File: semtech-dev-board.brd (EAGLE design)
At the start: 73.4 x 82.5 mm, 62 parts, among them Q1 BSS123, Q2 32MHz, U1 SEMTECH_SX1236, U2 QUALCOMM-TDK_B3588, U3 MIC5219 3.3V, U4 QUALCOMM-TDK_B3710

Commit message: Tuesday D/R
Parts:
- removed C24, C26, C28: 100nF, rcl:C0805
- removed TP7: TEST-POINT, low-gain-radio:2MM-TEST-POINT
- added TP3: TEST-POINT, low-gain-radio:2MM-TEST-POINT
- C11: value 22pF -> 100nF
- C12: value 4.7pF -> 100nF
- C13: value 8.2pF -> 100nF
- C14: value 2.7pF -> 8.2pF
- C15: value ?? -> 10nF
- C16: value 15pF -> 6.8pF
- C17: value ?? -> 5.6pF
- C18: value 6.8pF -> 100nF
- C19: value ?? -> 100nF
- C20: value 8.2pF -> 4.7pF
- C21: value 470pF -> 15pF
- C22: value 5.6pF -> 15pF
- C4: value 100nF -> 470pF
- C5: value 100nF -> 2.7pF
- C6: value 6pF -> 22pF
- C7: value 6pF -> 15pF
- C8: value 10nF -> 8.2pF
- JP1: device pinhead:1X07 -> pinhead:1X02
- JP2: device pinhead:1X04 -> pinhead:1X02
- JP3, JP5: device pinhead:1X02 -> pinhead:1X04
- JP4: device pinhead:1X04 -> pinhead:1X08
- L1: value 33nH -> 12nH; device rcl:L3230M -> rcl:L3225M
- L2: value 33nH -> 10nH; device rcl:L3230M -> rcl:L3225M
- L3: value 10nH -> 33nH; device rcl:L3230M -> rcl:L3225M
- L4: value 3.9nH -> 10nH; device rcl:L3230M -> rcl:L3225P
- L5: value 12nH -> 33nH; device rcl:L1812 -> rcl:L3225P
- L6: device rcl:L3230M -> rcl:L3225M
- L7: value 10nH -> 6.8nH; device rcl:L3230M -> rcl:L3225M
- L8: value 6.8nH -> 3.9nH; device rcl:L3230M -> rcl:L3225M
- R1: value 1k -> 0
- R5: value 0 -> 1k
- U1: value SEMTECH_SX1236 -> MIC5219 3.3V; device low-gain-radio:QFN28 -> SparkFun-IC-Power:SOT23-5
- U2: value QUALCOMM-TDK_B3588 -> QUALCOMM-TDK_B3710
- U3: value MIC5219 3.3V -> QUALCOMM-TDK_B3588; device SparkFun-IC-Power:SOT23-5 -> low-gain-radio:DCC6C
- U4: value QUALCOMM-TDK_B3710 -> SEMTECH_SX1236; device low-gain-radio:DCC6C -> low-gain-radio:QFN28
- moved U3 77.1 mm to (65.5, 75.9), turned to 180 degrees
- moved R2 56.7 mm to (18.3, 11.9), turned to 180 degrees
- moved U4 56.6 mm to (33.0, 23.6), turned to 0 degrees
- moved U2 54.1 mm to (11.4, 75.9)
- moved C22 53.7 mm to (26.2, 24.1), turned to 180 degrees
- moved R3 52.9 mm to (67.1, 40.9)
- moved JP2 51.1 mm to (70.9, 49.3), turned to 90 degrees
- moved C19 50.1 mm to (24.0, 26.5), turned to 180 degrees
- moved C7 42.7 mm to (26.6, 66.9)
- moved C18 39.3 mm to (28.4, 31.8), turned to 90 degrees
- moved C6 38.8 mm to (27.6, 59.5), turned to 90 degrees
- moved C13 38.7 mm to (39.6, 21.3), turned to 270 degrees
- moved JP4 38.4 mm to (37.6, 2.03)
- moved C5 37.3 mm to (27.6, 63.6), turned to 90 degrees
- moved JP3 35.4 mm to (36.6, 40.4), turned to 0 degrees
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- renumbered C23 to C3, C27 to C1, CF1 to P5, Q2 to Y1, S2 to S1, U$1 to P1, U$2 to P2, U$3 to P3, U$4 to P4
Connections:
- removed net DIO0: JP1.2, U1.8
- removed net DIO1: JP1.3, U1.9
- removed net DIO2: JP1.4, U1.10
- removed net DIO3: JP1.5, U1.11
- removed net DIO4: JP1.6, U1.12
- removed net DIO5: JP1.7, U1.13
- new net N$2: JP4.8, U4.13
- new net N$4: JP4.7, U4.12
- new net N$6: JP4.6, U4.11
- new net N$7: JP4.5, U4.10
- new net N$8: JP4.4, U4.9
- new net N$9: JP4.3, U4.8
- net +3V3: now also R4.2, R5.2, TP6.1, U1.5; no longer R1.2, R3.2, TP5.1, U3.5
- net BP: now also C4.1, U1.4; no longer C21.1, U3.4
- net GND: now also C11.2, C13.2, C15.2, C17.2, C19.2, JP1.2, JP2.2, U1.2, U3.P$1, U3.P$3, U3.P$4, U3.P$6, U4.0, U4.15, U4.23, U4.26; no longer C24.2, C26.2, C28.2, C5.2, C6.2, JP3.2, JP5.2, U1.0, U1.15, U1.23, U1.26, U3.2, U4.P$1, U4.P$3, U4.P$4, U4.P$6
- net HFO_PA_HEAD: now also C15.1, JP3.4, L5.2; no longer C9.1, JP4.4, L2.2
- net LED+: now also R3.1; no longer R2.1
- net LFO_PA_HEAD: now also C9.1, JP3.1, L3.2; no longer C8.1, JP4.1, L1.2
- net N$1: now also R2.1, TP4.1, U1.3; no longer R5.1, TP1.1, U3.3
- net N$5: now also U2.P$5; no longer U4.P$5
- net PA_BOOST: now also TP2.1, U4.27; no longer TP7.1, U1.27
- net RFI_HF: now also U3.P$2, U4.21; no longer U1.21, U2.P$2
- net RFI_HF_ANT: now also U3.P$5; no longer U2.P$5
- net RFI_LF: now also U2.P$2, U4.1; no longer U1.1, U4.P$2
- net RFO_HF: now also L8.2, U4.22; no longer L4.2, U1.22
- net RFO_HF_1: now also C14.2; no longer C13.2, C15.1
- net RFO_HF_2: now also C16.1, L7.2; no longer C15.2, C18.1, C19.1, L8.2
- net RFO_HF_OUT: now also C17.1, L7.1; no longer C19.2, C22.1, L8.1
- net RFO_HF_PA: now also C14.1, C20.1, L5.1, L8.1; no longer C12.1, C13.1, L2.1, L4.1
- net RFO_LF: now also L4.1, U4.28; no longer L3.1, U1.28
- net RFO_LF_1: now also C5.1, C6.2, L1.2; no longer C11.2, C14.1, L5.2
- net RFO_LF_2: now also C5.2, C7.1, L1.1, L2.2; no longer C14.2, C16.1, C17.1, L5.1, L7.2
- net RFO_LF_OUT: now also C8.1, L2.1; no longer C17.2, C20.1, L7.1
- net RFO_LF_PA: now also C6.1, L3.1, L4.2; no longer C11.1, L1.1, L3.2
- net RXTX: now also JP2.1, JP4.2, U4.20; no longer JP1.1, JP3.1, U1.20
- net SPI_MISO: now also JP5.2, U4.17; no longer JP2.2, U1.17
- net SPI_MOSI: now also JP5.3, U4.18; no longer JP2.3, U1.18
- net SPI_NSS: now also JP5.4, U4.19; no longer JP2.4, U1.19
- net SPI_SCK: now also JP5.1, U4.16; no longer JP2.1, U1.16
- net SX1236_RST: now also JP4.1, R5.1, TP1.1, U4.7; no longer R1.1, TP4.1, U1.7
- net VBAT: now also C11.1, C12.1, C13.1, R3.2, R4.1, U4.14, U4.24, U4.3; no longer C2.1, C24.1, C26.1, R2.2, R3.1, U1.14, U1.24, U1.3
- net VREG_IN: now also C2.1, R1.2, R2.2, TP5.1, U1.1; no longer C28.1, R4.2, R5.2, TP6.1, U3.1
- net VR_ANA: now also C18.1, U4.2; no longer C4.1, U1.2
- net VR_DIG: now also C19.1, U4.4; no longer C5.1, U1.4
- net VR_PA: now also JP3.2, JP3.3, U4.25; no longer JP4.2, JP4.3, U1.25
- net V_IN: now also JP1.1, R1.1, TP3.1; no longer JP5.1, R4.1, TP2.1
- net XTALA: now also C22.1, U4.5; no longer C7.1, U1.5
- net XTALB: now also C21.1, U4.6; no longer C6.1, U1.6
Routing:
- net DIO5: track 24.7 -> 0.00 mm
- net DIO4: track 23.9 -> 0.00 mm
- net DIO0: track 23.2 -> 0.00 mm
- net DIO3: track 23.1 -> 0.00 mm
- net DIO1: track 22.4 -> 0.00 mm
- net DIO2: track 22.3 -> 0.00 mm
- net RFO_HF_2: track 10.5 -> 6.00 mm
- net VREG_IN: track 11.8 -> 15.6 mm
- net RFO_LF_OUT: track 10.4 -> 7.95 mm
- net RFO_HF_OUT: track 10.3 -> 7.93 mm
- net RXTX: track 141.6 -> 140.6 mm
- net RFO_LF_1: track 5.46 -> 5.97 mm
- added copper zone on layer 2, net GND
- added copper zone on layer 15, net VBAT
- removed copper zone on layer 2, net VBAT
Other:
- board size 73.4 x 82.5 mm -> 73.2 x 82.2 mm

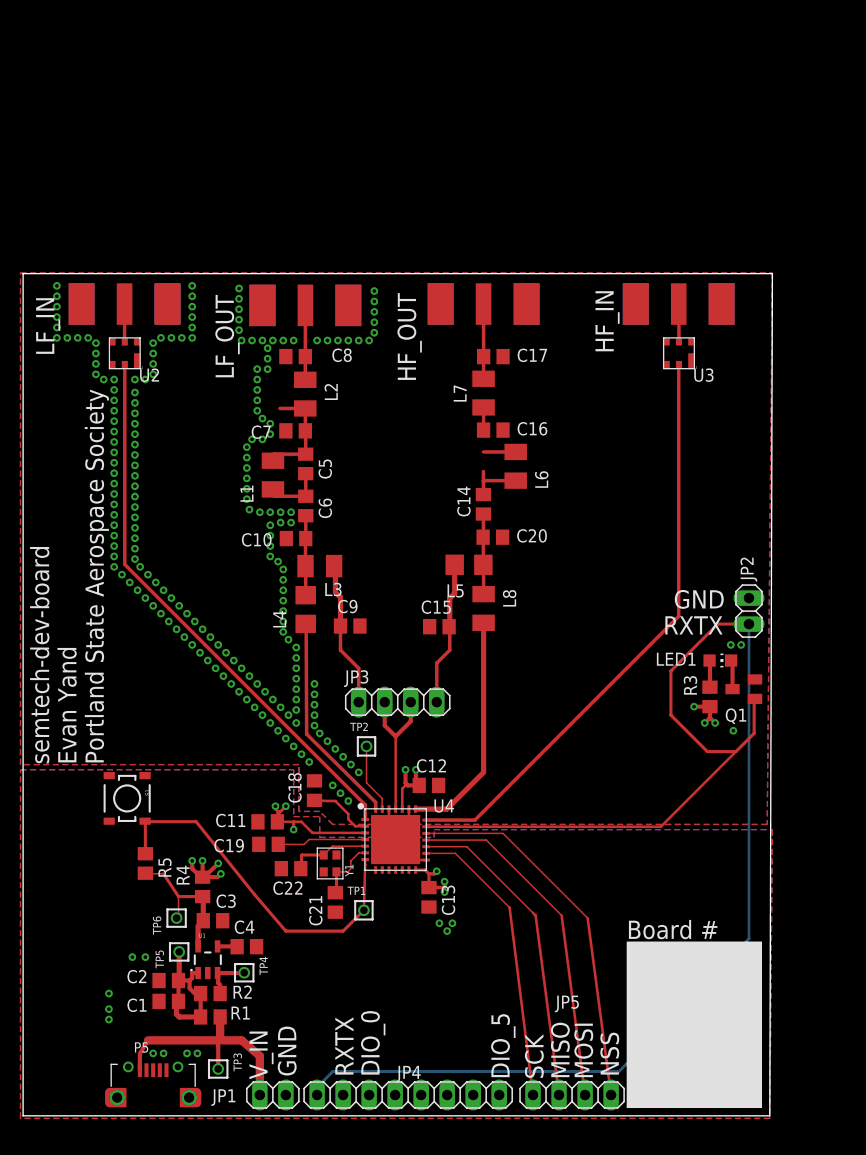
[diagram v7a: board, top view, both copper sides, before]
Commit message: reworked board based on feedback, needs mounting holes
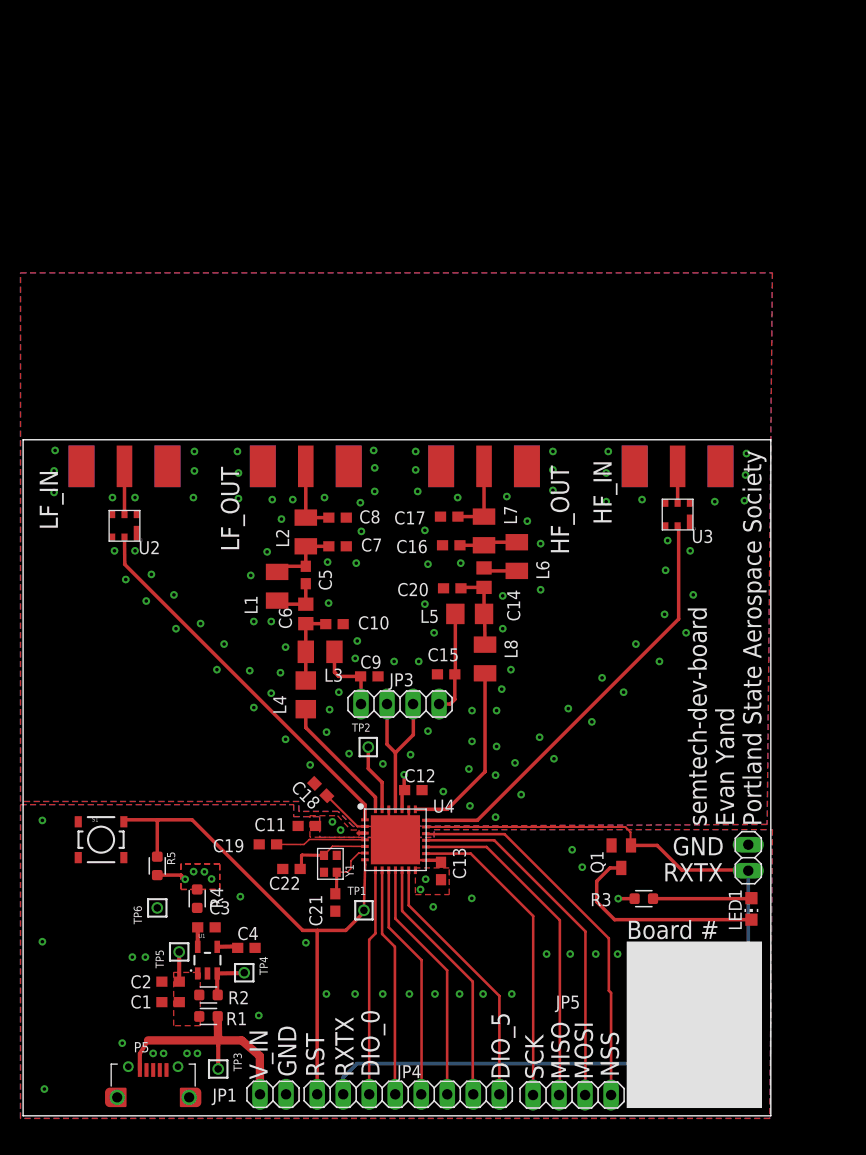
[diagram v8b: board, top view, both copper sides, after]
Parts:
- removed P1: SMAJ716-ND, psas_c3_team05:SMAJ716-ND
- added RFO_LF_IN: SMAJ716-ND, psas_c3_team05:SMAJ716-ND
- added U$1, U$2, U$3, U$4, U$5, U$6, U$7: (no value), oresat-eagle:SCOPE_CLIP
- C1, C10, C11, C12, C13, C15, C16, C17, C18, C19, C2, C20, C21, C22, C3, C4, C5, C7, C8, C9: device rcl:C0805 -> rcl_custom:C0603
- R1, R2, R3, R4, R5: device rcl:R0805 -> rcl_custom:.0603-A
- moved LED1 24.4 mm to (71.1, 20.2), turned to 180 degrees
- moved JP2 24.1 mm to (70.8, 25.2)
- moved R3 20.7 mm to (60.6, 21.2), turned to 180 degrees
- moved Q1 20.3 mm to (58.4, 25.3), turned to 180 degrees
- moved U2 16.8 mm to (11.4, 59.1)
- moved C8 16.2 mm to (30.7, 58.4), turned to 0 degrees
- moved C17 16.2 mm to (41.6, 58.5), turned to 180 degrees
- moved P4 15.8 mm to (63.9, 62.9)
- moved P3 15.8 mm to (45.0, 62.9)
- moved U3 15.7 mm to (65.4, 60.2)
- moved P2 15.7 mm to (27.6, 62.9)
- moved L2 13.5 mm to (27.6, 57.0)
- moved L7 13.5 mm to (45.0, 57.1)
- moved C7 12.0 mm to (30.7, 55.6), turned to 0 degrees
- moved C16 12.0 mm to (41.8, 55.7), turned to 180 degrees
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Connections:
- net N$2 renamed DIO5
- net N$4 renamed DIO4
- net N$6 renamed DIO3
- net N$7 renamed DIO2
- net N$8 renamed DIO1
- net N$9 renamed DIO0
- removed net N$5: P1.P$3, U2.P$5
- removed net VBAT: C11.1, C12.1, C13.1, R3.2, R4.1, U4.14, U4.24, U4.3
- new net RFI_LF_ANT: RFO_LF_IN.P$3, U2.P$5
- new net VREG_OUT: C3.1, R4.1, TP6.1, U1.5
- net +3V3: now also C11.1, C12.1, C13.1, R3.2, U4.14, U4.24, U4.3; no longer C3.1, TP6.1, U1.5
- net GND: now also RFO_LF_IN.GND1, RFO_LF_IN.GND2, RFO_LF_IN.GND3, RFO_LF_IN.GND4; no longer P1.GND1, P1.GND2, P1.GND3, P1.GND4
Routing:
- net RXTX: track 140.6 -> 89.2 mm
- net VBAT: track 37.5 -> 0.00 mm, vias 15 -> 0
- net DIO5: track 0.00 -> 25.7 mm
- net DIO4: track 0.00 -> 24.9 mm
- net DIO3: track 0.00 -> 24.1 mm
- net DIO2: track 0.00 -> 23.3 mm
- net DIO1: track 0.00 -> 22.5 mm
- net DIO0: track 0.00 -> 22.1 mm
- net SX1236_RST: track 35.4 -> 53.5 mm
- net LED-: track 2.85 -> 20.8 mm
- net RFI_LF: track 54.1 -> 37.3 mm
- net RFI_HF: track 57.5 -> 41.9 mm
- net VREG_IN: track 15.6 -> 2.91 mm
- net RFO_LF: track 20.9 -> 12.6 mm
- net LED+: track 2.62 -> 9.62 mm
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- added copper zone on layer 1, net +3V3
- added copper zone on layer 15, net +3V3
- added copper zone on layer 1, net VREG_IN
- removed copper zone on layer 15, net VBAT
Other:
- board size 73.2 x 82.2 mm -> 73 x 66 mm
- board text added: "RST"
